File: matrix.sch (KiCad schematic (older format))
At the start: 153 parts

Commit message: Remap symbols
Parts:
- D01, D02, D03, D04, D05, D06, D07, D08, D09, D10, D11, D12, D13, D14, D15, D16, D17, D18, D19, D21, D22, D23, D24, D26, D27, D28, D29, D30, D31, D32, D33, D34, D36, D37, D38, D39, D41, D42, D43, D44, D46, D47, D48, D49, D50, D51, D52, D53, D54, D55, D56, D57, D58, D59, D60, D61, D62, D63, D64, D65, D66, D67, D68, D69, D70: symbol DIODE -> keyboard-rescue:DIODE-device
- DC1, DC2, DC3: symbol LED -> keyboard-rescue:LED-device
- R4: symbol R -> keyboard-rescue:R-device
- S01, S02, S03, S031, S04, S041, S05, S0512, S06, S07, S08, S09, S10, S101, S102, S11, S12, S13, S14, S15, S151, S16, S17, S18, S19, S21, S22, S23, S24, S26, S27, S28, S29, S30, S301, S302, S31, S32, S33, S34, S36, S37, S38, S39, S41, S42, S43, S44, S46, S47, S48, S49, S50, S51, S52, S53, S54, S55, S552, S56, S57, S58, S59, S60, S601, S602, S61, S62, S63, S64, S641, S65, S6512, S66, S661, S67, S68, S681, S682, S69, S691, S692, S70, S7012: symbol MX1A -> keyboard-rescue:MX1A-mx1a-simple

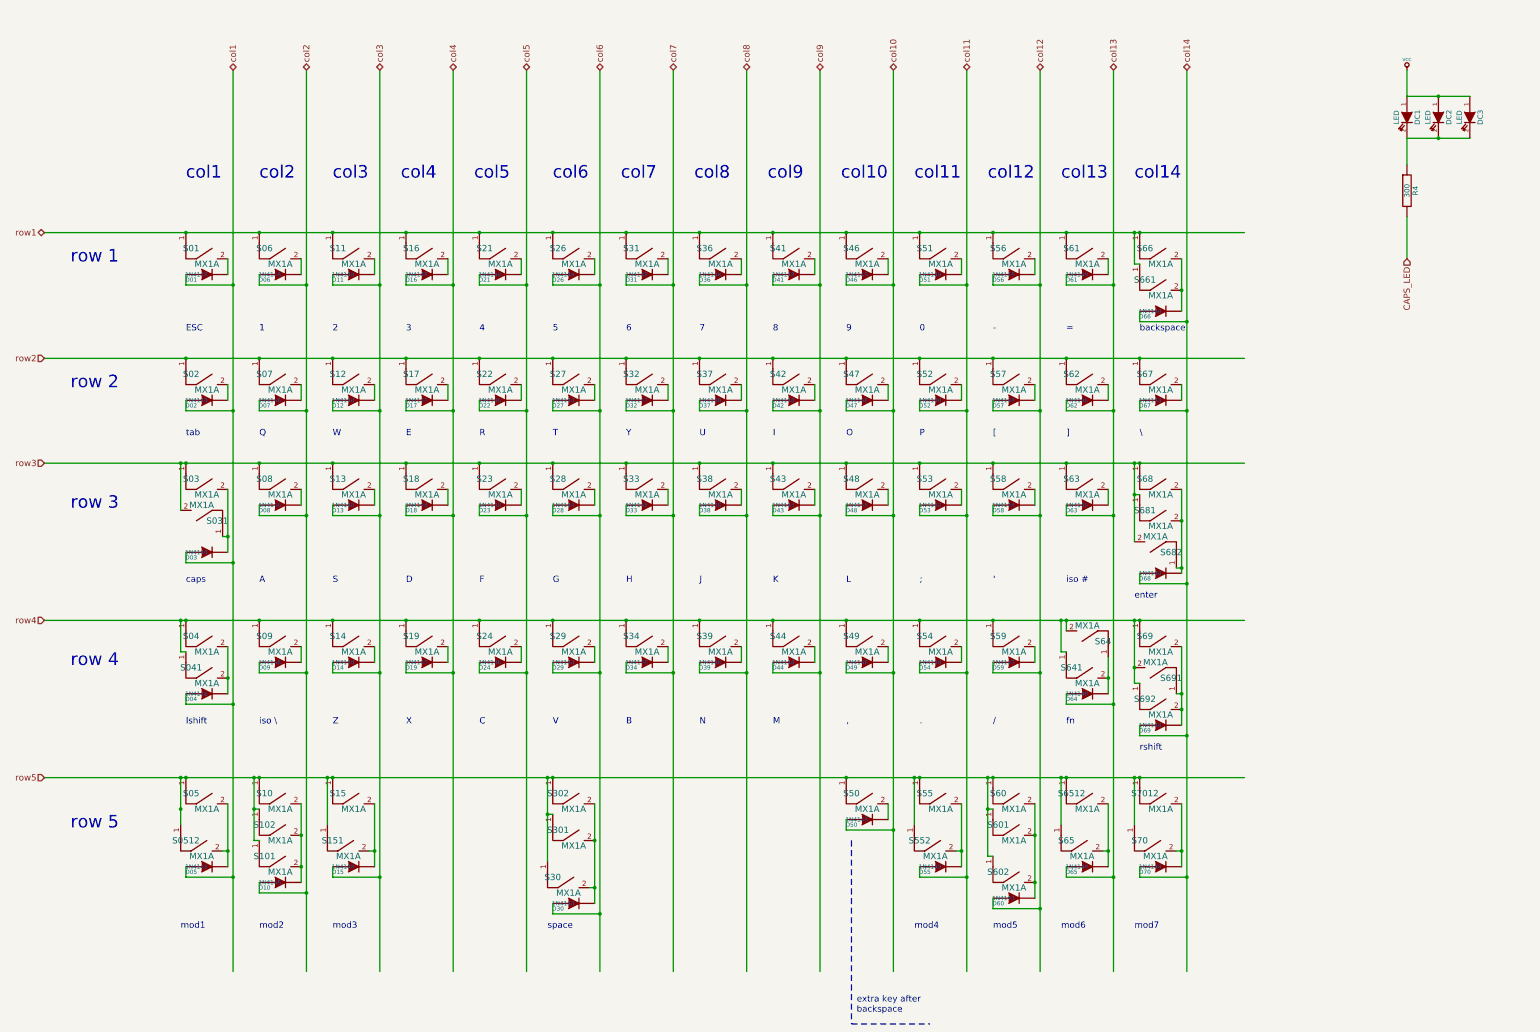
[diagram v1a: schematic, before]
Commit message: Add nRF52840 MCU sheet
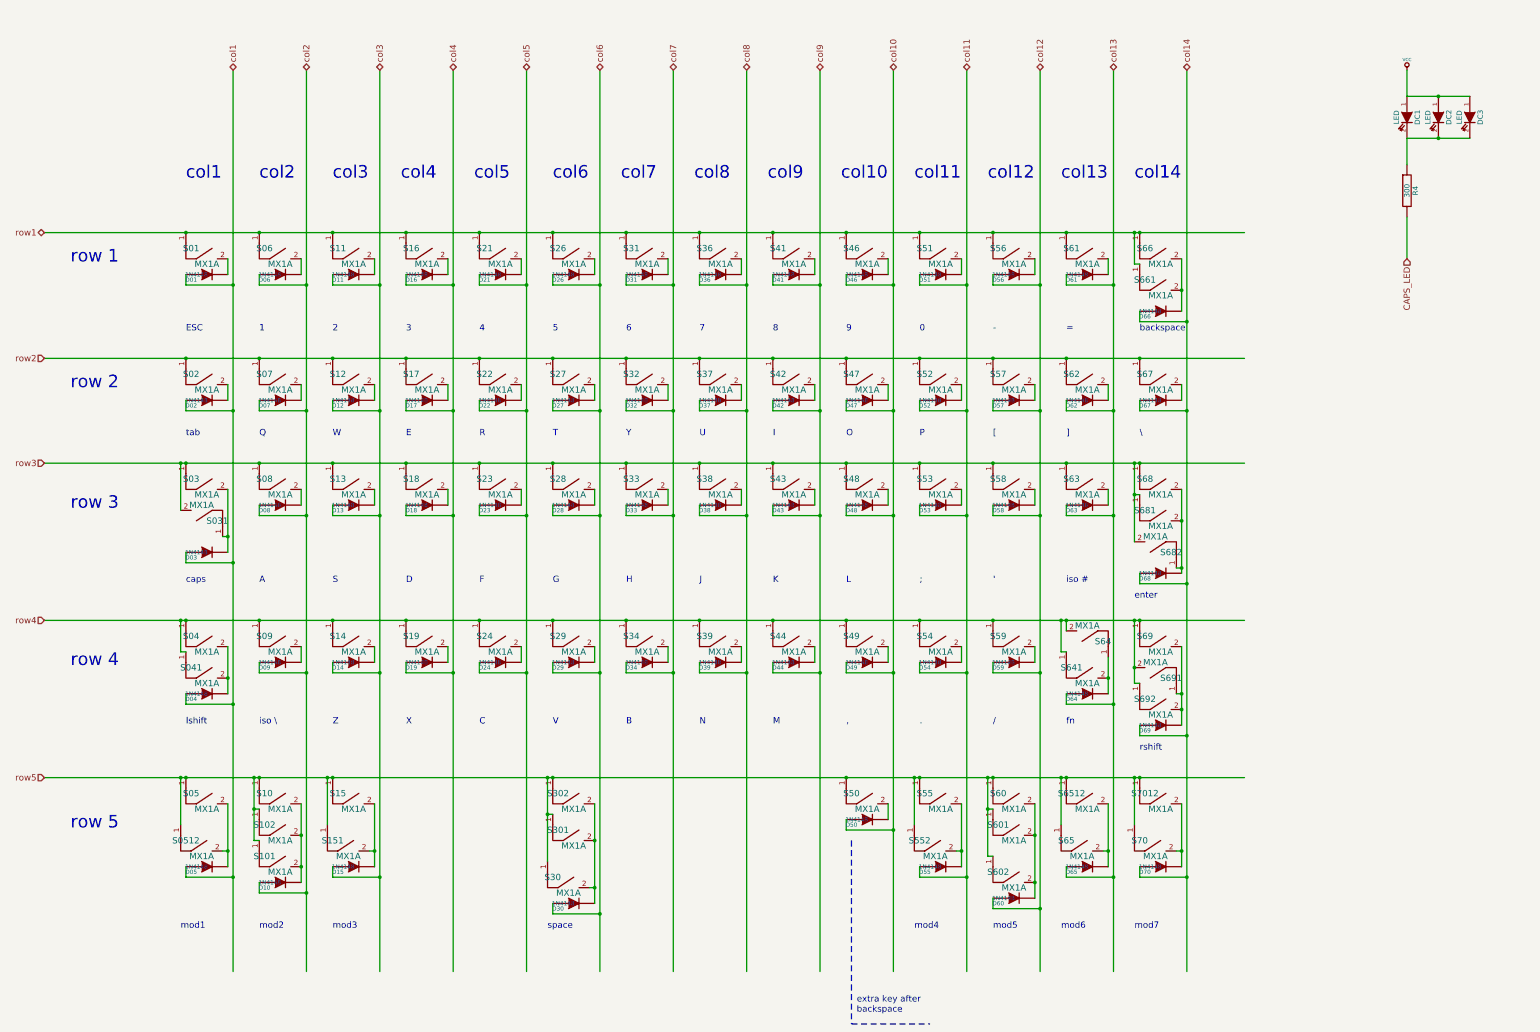
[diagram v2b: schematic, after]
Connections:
- wire segments 254 -> 423
